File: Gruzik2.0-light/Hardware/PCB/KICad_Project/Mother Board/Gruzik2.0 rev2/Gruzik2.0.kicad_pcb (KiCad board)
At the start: 4 copper layers, 126.6 x 37.7 mm, 50 parts, among them U1 STM32F103C8T6, U2 LM1117MP-3.3, U3 LM1117MP-5.0, U4 TB6612FNG, U5 TB6612FNG, U7 HC-05, Y1 8MHz

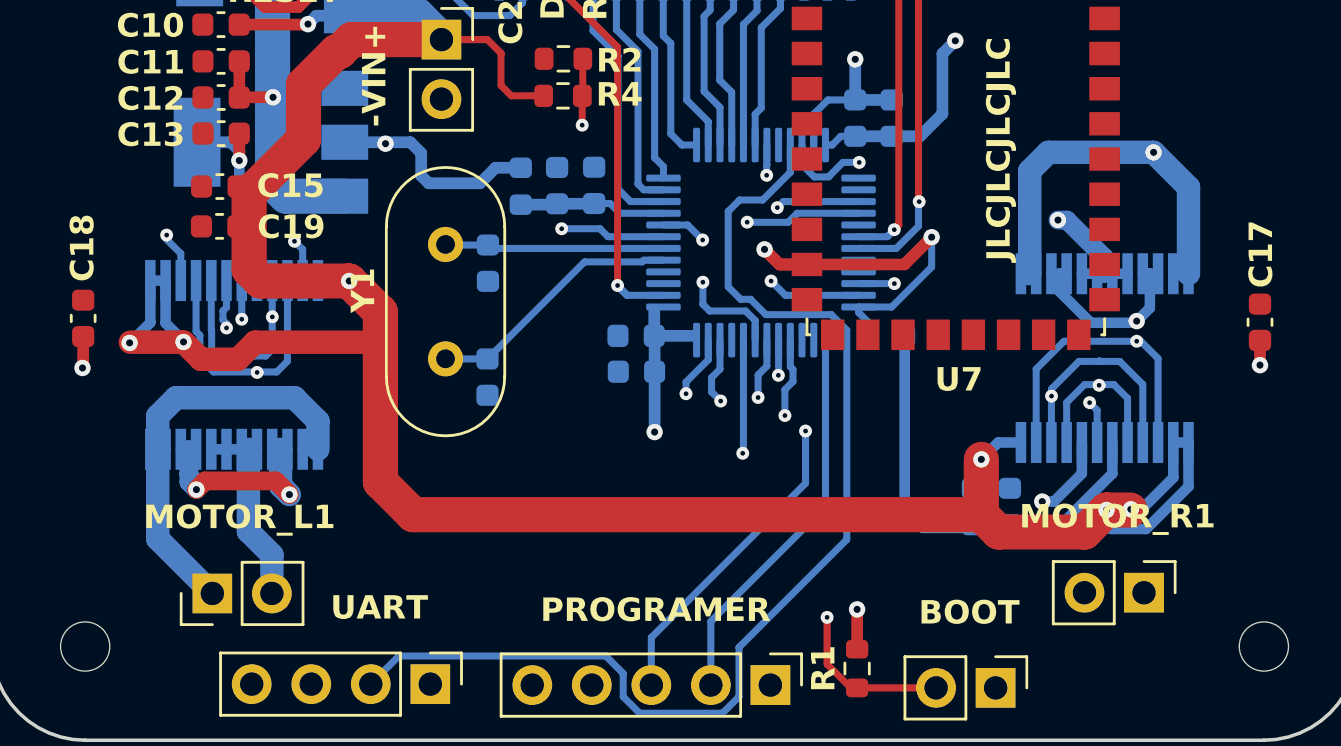
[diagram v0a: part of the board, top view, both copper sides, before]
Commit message: 2.1.6
motherboard rev 2 update
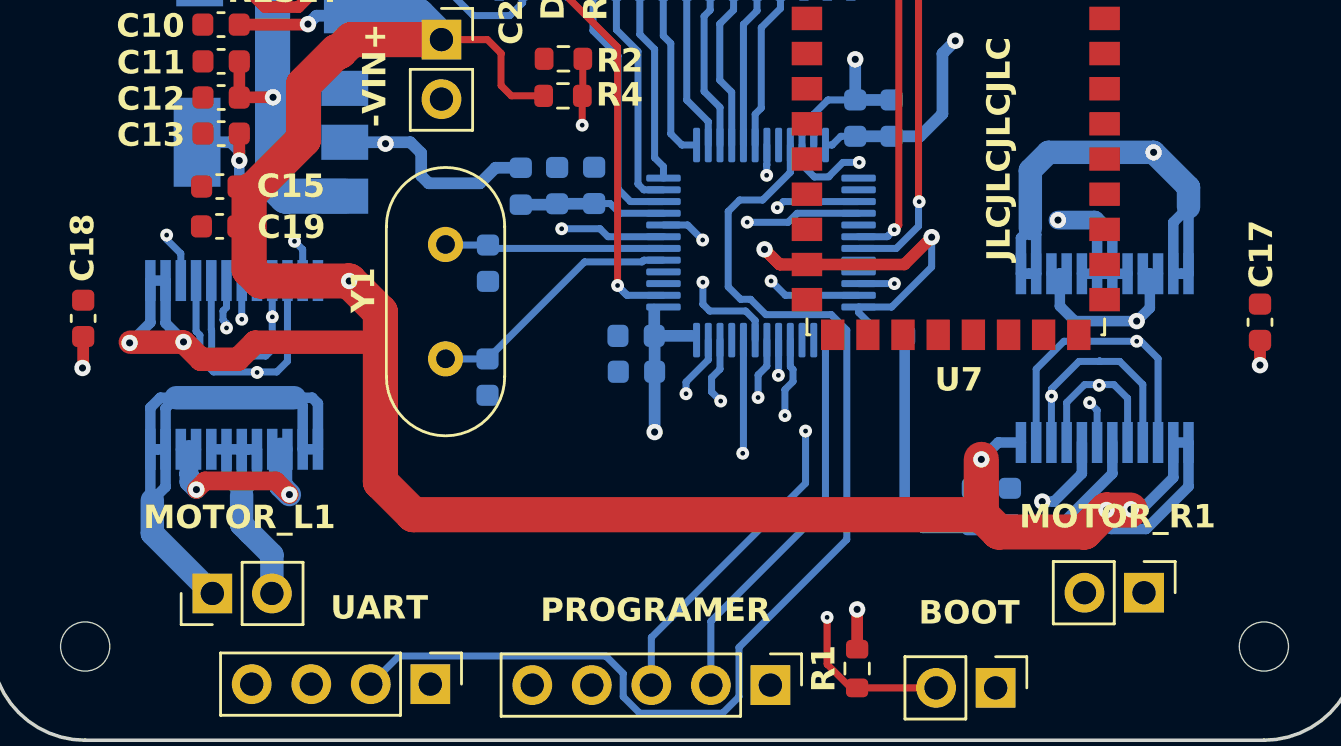
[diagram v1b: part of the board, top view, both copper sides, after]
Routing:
- net Net-(MOTOR_L1-Pin_1): track 18.6 -> 26.8 mm
- net Net-(MOTOR_R1-Pin_1): track 40.4 -> 45.7 mm
- net Net-(MOTOR_L1-Pin_2): track 8.51 -> 13.1 mm
- net Net-(MOTOR_R1-Pin_2): track 29.1 -> 32.0 mm

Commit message: 2.1.7
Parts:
- renumbered GRUZIK2.0 to GRUZIK2.1
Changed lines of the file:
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@@
     (property "ki_keywords" "connector")
     (attr smd)
-    (fp_text reference "GRUZIK2.0" (at 0.14 -1.74) (layer "B.SilkS" knockout)
+    (fp_text reference "GRUZIK2.1" (at 0.14 -1.74) (layer "B.SilkS" knockout)
         (effects (font (size 1 1) (thickness 0.25) bold) (justify mirror))
     )
